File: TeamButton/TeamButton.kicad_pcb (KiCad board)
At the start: 2 copper layers, 79.9 x 70 mm, 7 parts, among them J1 RJ45, SW1 10T85 Microswitch, SW2 10T85 Microswitch

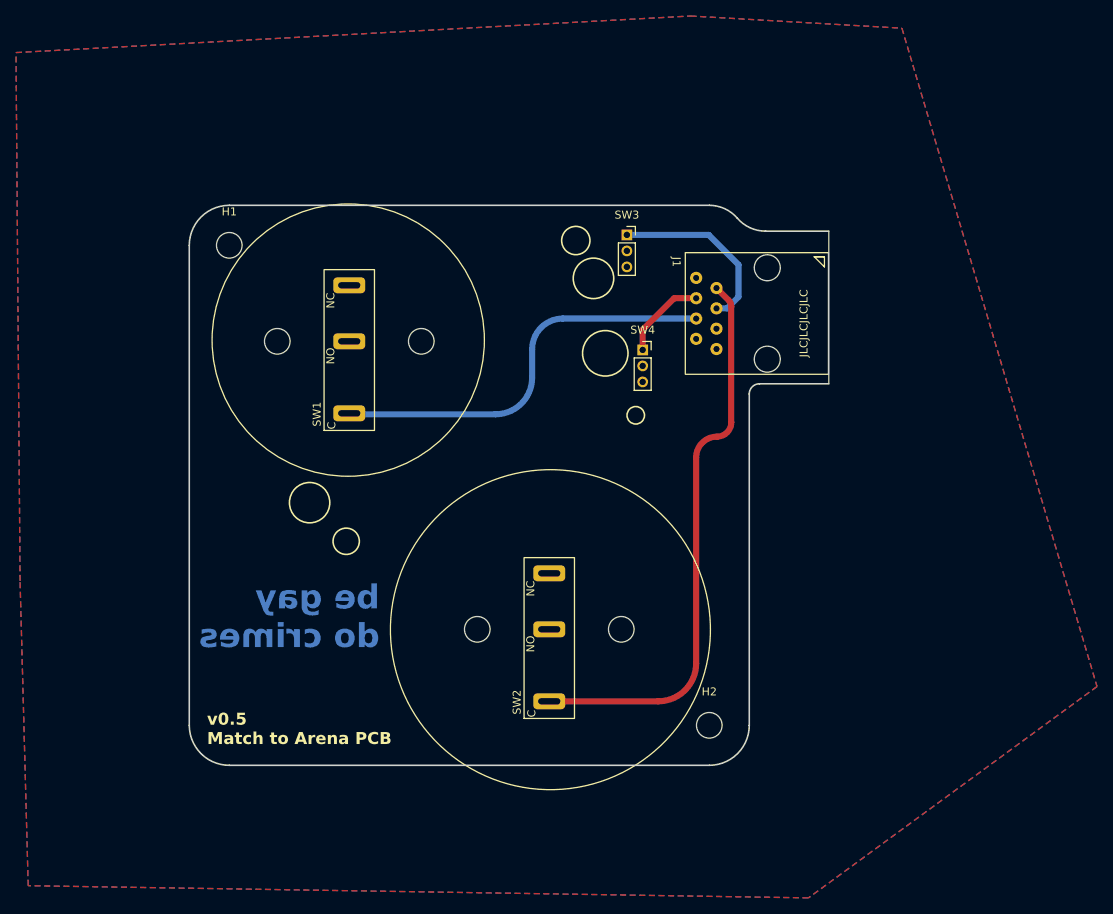
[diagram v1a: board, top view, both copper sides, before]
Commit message: Update ArenaController footprints to be over the edge and line up with the printed enclosure.
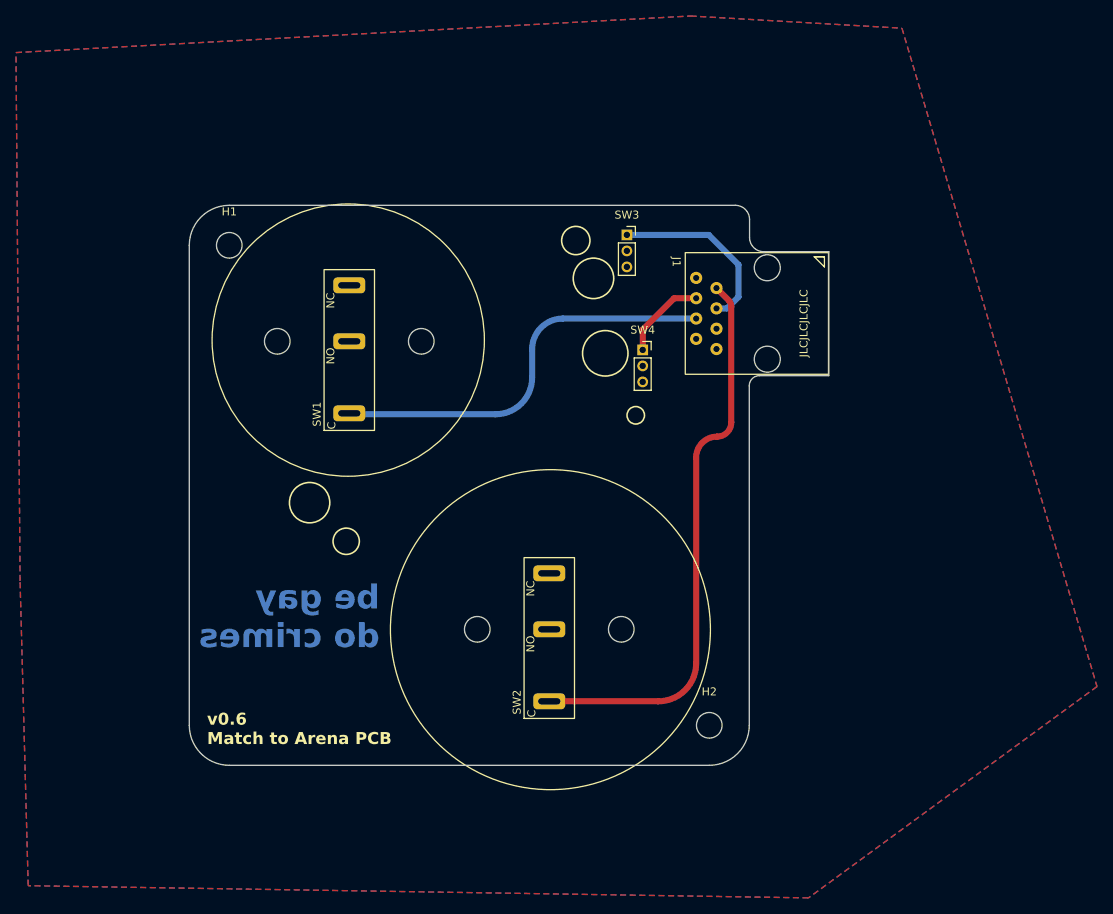
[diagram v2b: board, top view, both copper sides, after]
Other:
- outline, holes or cut-outs redrawn
- board text added: "v0.6 Match to Arena PCB"
- board text removed: "v0.5 Match to Arena PCB"

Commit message: Release 7/19/23
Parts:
- removed SW3, SW4: ~, Connector_PinSocket_2.00mm:PinSocket_1x03_P2.00mm_Vertical
- added J2: Conn_01x08_MountingPin, Connector_PinSocket_2.54mm:PinSocket_1x08_P2.54mm_Horizontal, F.Cu at (114.6, 47.5)
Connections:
- J1 pad 1: unconnected-(J1-Pad1) -> Net-(J2-Pin_1)
- J1 pad 2: unconnected-(J1-Pad2) -> Net-(J2-Pin_2)
- J1 pad 3: unconnected-(J1-Pad3) -> Net-(J2-Pin_3)
- J1 pad 5: /P_RST -> Net-(J2-Pin_5)
- J1 pad 6: /P_PAUSE -> Net-(J2-Pin_6)
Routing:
- net Net-(J2-Pin_1): track 0.00 -> 32.7 mm
- net Net-(J2-Pin_2): track 0.00 -> 27.1 mm
- net Net-(J2-Pin_3): track 0.00 -> 26.6 mm
- net /P_RST: track 22.9 -> 0.00 mm
- net Net-(J2-Pin_5): track 0.00 -> 20.5 mm
- net /P_START: track 51.4 -> 71.3 mm
- net Net-(J2-Pin_6): track 0.00 -> 14.9 mm
- net /P_END: track 70.8 -> 85.7 mm
- net /P_PAUSE: track 10.8 -> 0.00 mm
- net GND: vias 0 -> 11
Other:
- board text removed: "PAUSE"
- board text removed: "RESET"

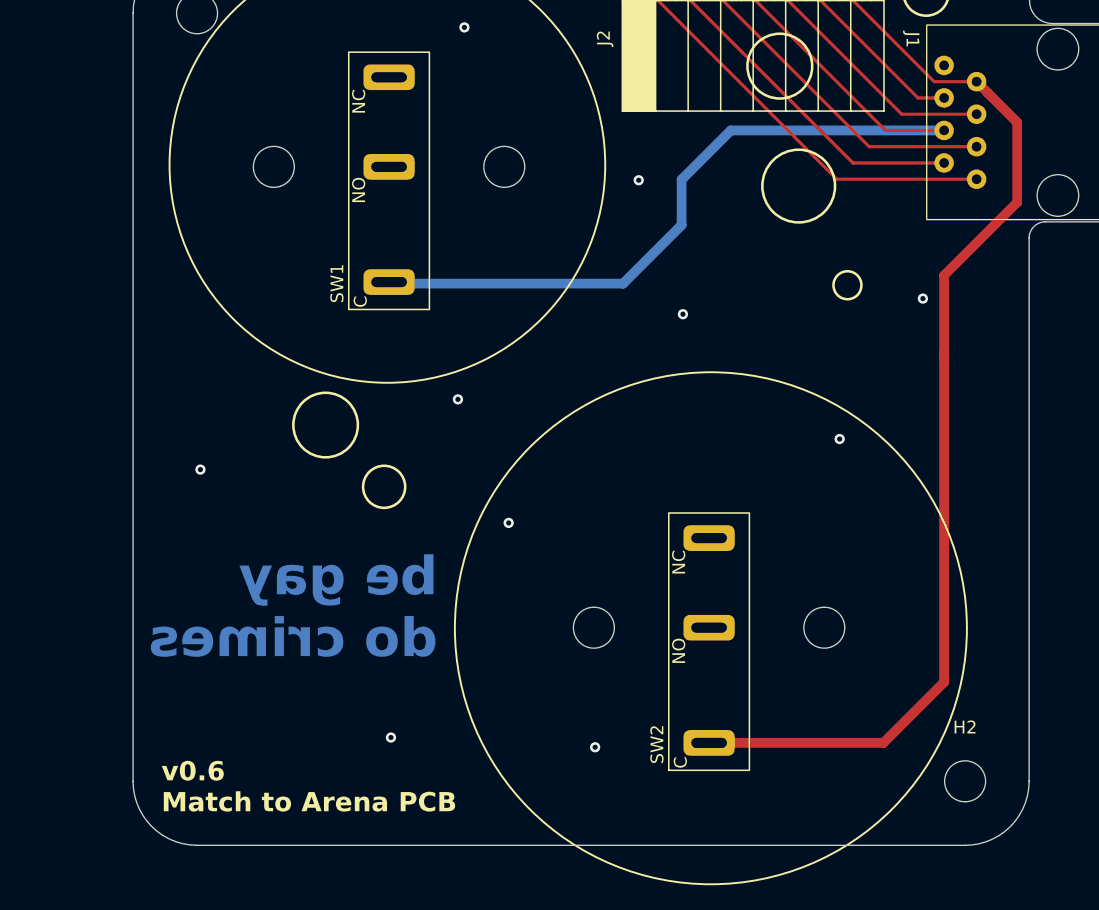
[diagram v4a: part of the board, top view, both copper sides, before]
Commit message: Changed output tool to fix missing drill files, at least in theory.
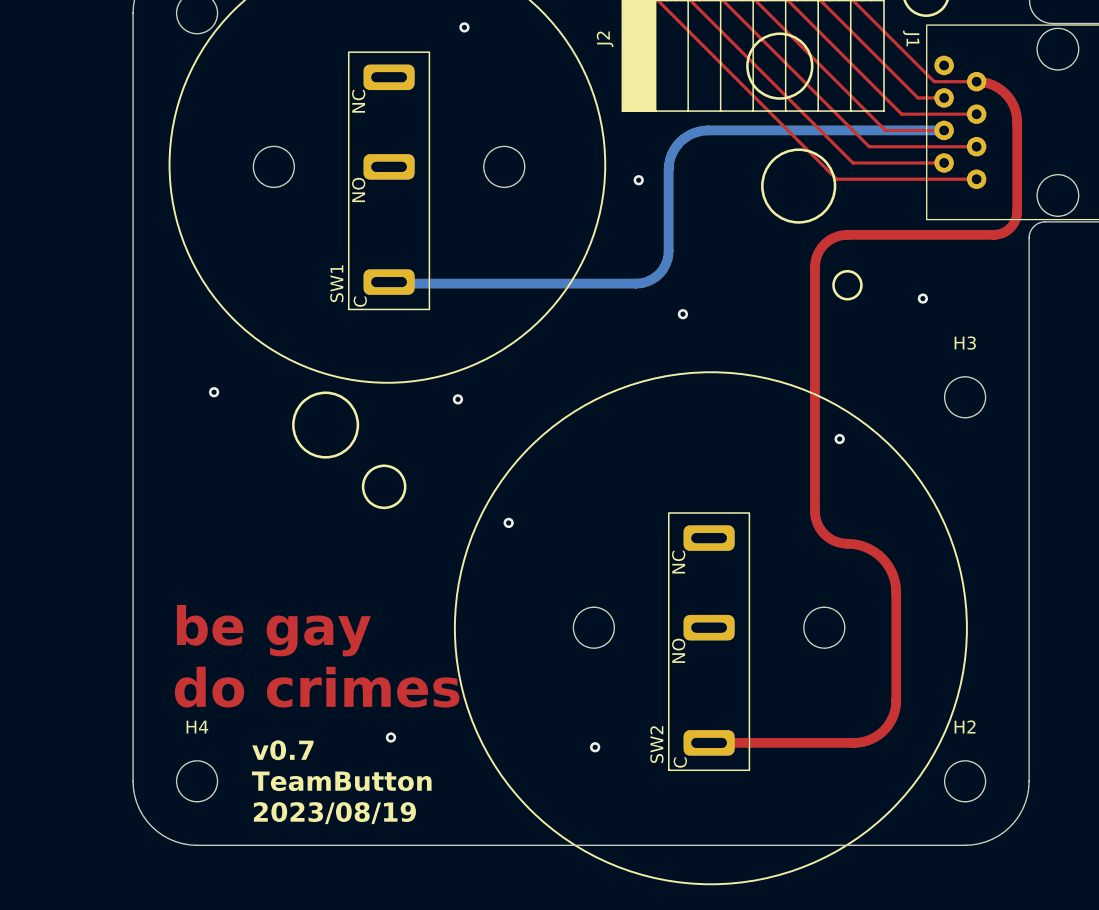
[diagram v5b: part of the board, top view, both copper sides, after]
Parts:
- added H3: MountingHole, MountingHole:MountingHole_3.2mm_M3, F.Cu at (140.0, 80.0)
- added H4: MountingHole, MountingHole:MountingHole_3.2mm_M3, F.Cu at (80.0, 110.0)
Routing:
- net /P_END: track 85.7 -> 97.9 mm
- net /P_START: track 71.3 -> 73.6 mm
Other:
- board text added: "v0.7 TeamButton 2023/08/19"
- board text removed: "v0.6 Match to Arena PCB"

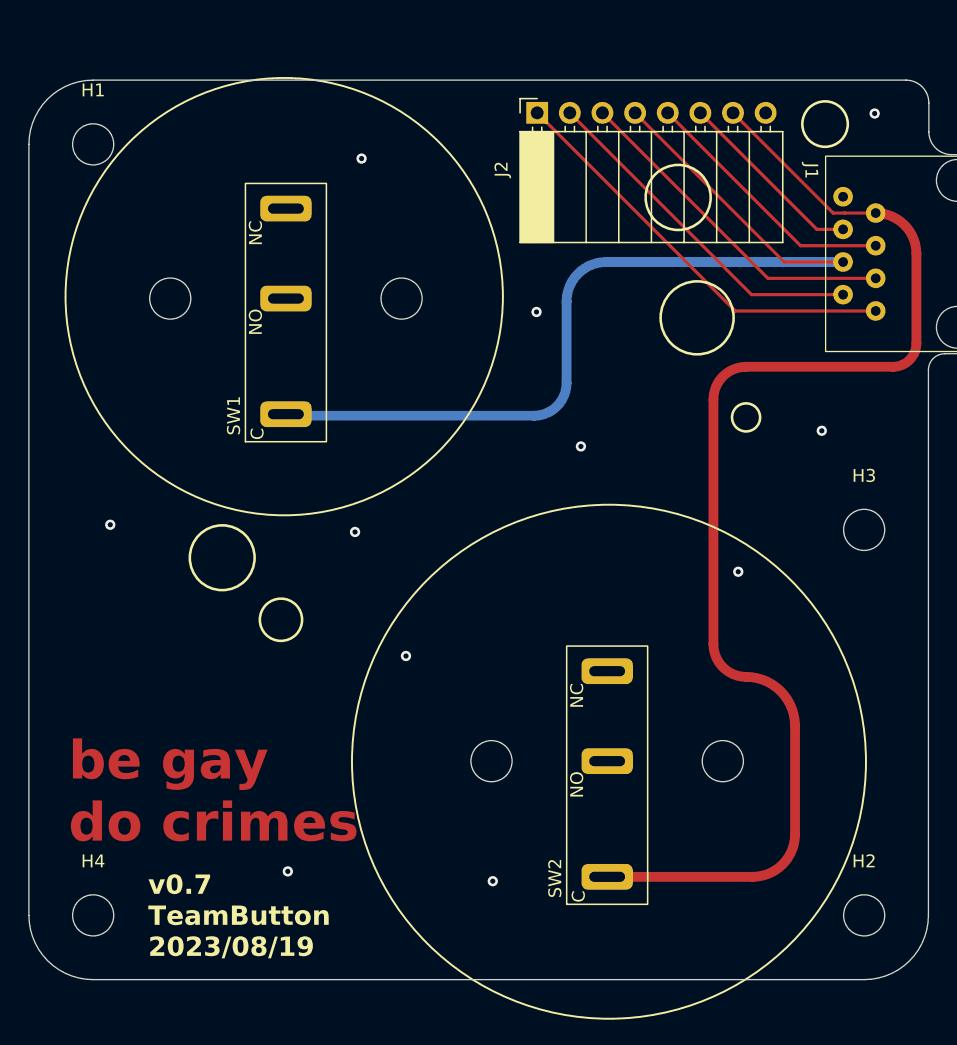
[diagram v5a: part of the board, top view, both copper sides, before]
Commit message: Fix footprint issue with the LM2596 and re-spin for next use.
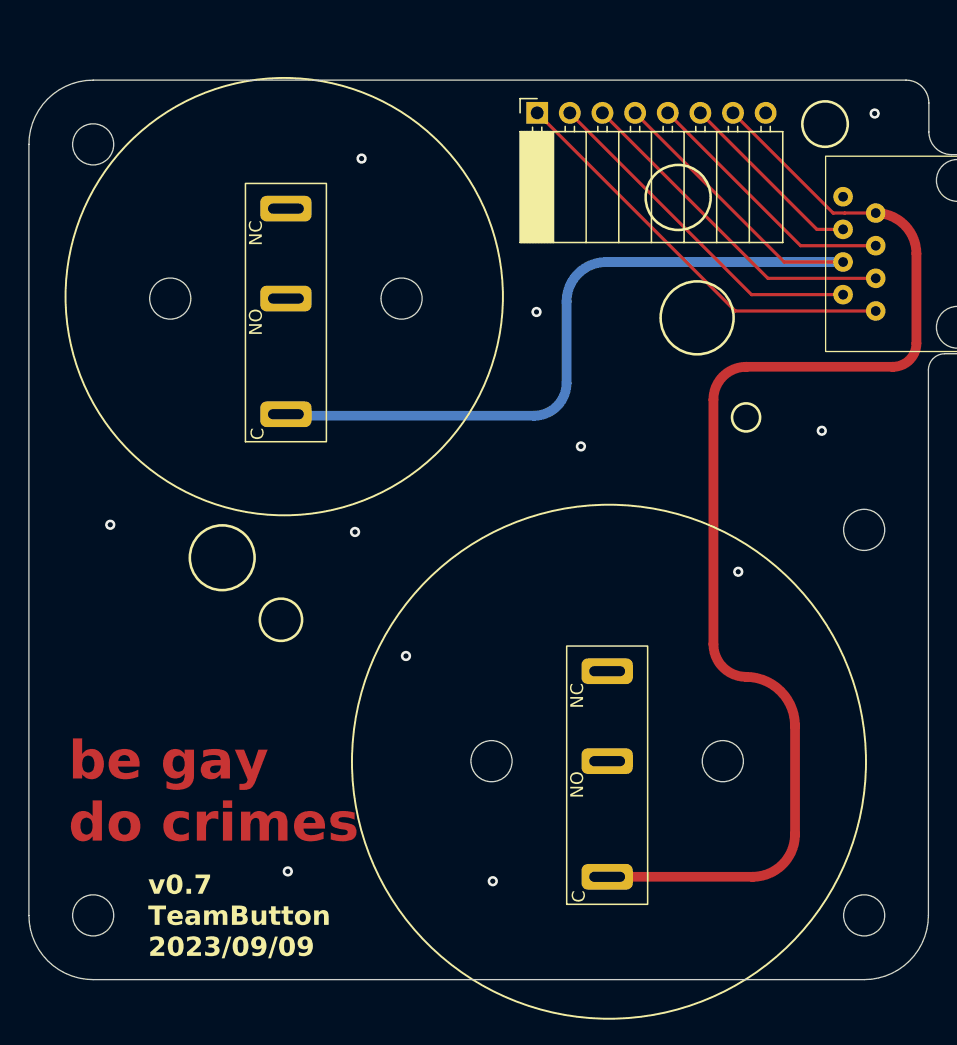
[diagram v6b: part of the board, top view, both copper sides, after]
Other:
- board text added: "v0.7 TeamButton 2023/09/09"
- board text removed: "v0.7 TeamButton 2023/08/19"
